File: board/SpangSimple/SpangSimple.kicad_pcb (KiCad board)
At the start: 2 copper layers, 37.5 x 43.5 mm, 3 parts

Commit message: sending off gerbers
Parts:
- removed the G*** at (182.4, 126.5) (x2)
- added BT1: Battery_Cell, SpangSimple:COINCELL_20MM_HANDSOLDER, B.Cu at (152.8, 102.2)
- added D1: LED, SpangSimple:LED_0805_HandSoldering, F.Cu at (153.9, 106.1)
- added D2: LED, SpangSimple:LED_0805_HandSoldering, F.Cu at (155.0, 107.8)
- added D3: LED, SpangSimple:LED_0805_HandSoldering, F.Cu at (156.6, 109.6)
- added D4: LED, SpangSimple:LED_0805_HandSoldering, F.Cu at (157.5, 111.3)
- added D5: LED, SpangSimple:LED_0805_HandSoldering, F.Cu at (156.4, 112.9)
- added D6: D_Schottky, Diodes_SMD:SOD-323_HandSoldering, B.Cu at (151.9, 116.9)
- added D7: LED, SpangSimple:LED_0805_HandSoldering, B.Cu at (148.1, 82.3)
- added D8: LED, SpangSimple:LED_0805_HandSoldering, B.Cu at (140.0, 91.4)
- added F1: Fuse, Fuse_Holders_and_Fuses:Fuse_SMD1206_HandSoldering, B.Cu at (145.5, 114.6)
- added G***: LOGO, LOGO, F.Cu at (182.5, 126.4)
- added G***: LOGO, LOGO, F.Cu at (182.4, 126.5)
- added R1: R, Resistors_SMD:R_0805_HandSoldering, B.Cu at (169.1, 99.8)
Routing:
- net +BATT: track 0.00 -> 80.7 mm, vias 0 -> 1
- net Net-(BT1-Pad1): track 0.00 -> 53.4 mm
- net Net-(D7-Pad1): track 0.00 -> 44.9 mm
- net GND: track 0.00 -> 29.7 mm, vias 0 -> 3
- net Net-(D6-Pad2): track 0.00 -> 4.26 mm
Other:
- net class Default: clearance 0.1 -> 0.2032
- rule trace_clearance: 0.1 -> 0.2032
- board text added: "grant"
- board text added: "jerge"
- board text added: "sincity assassin"

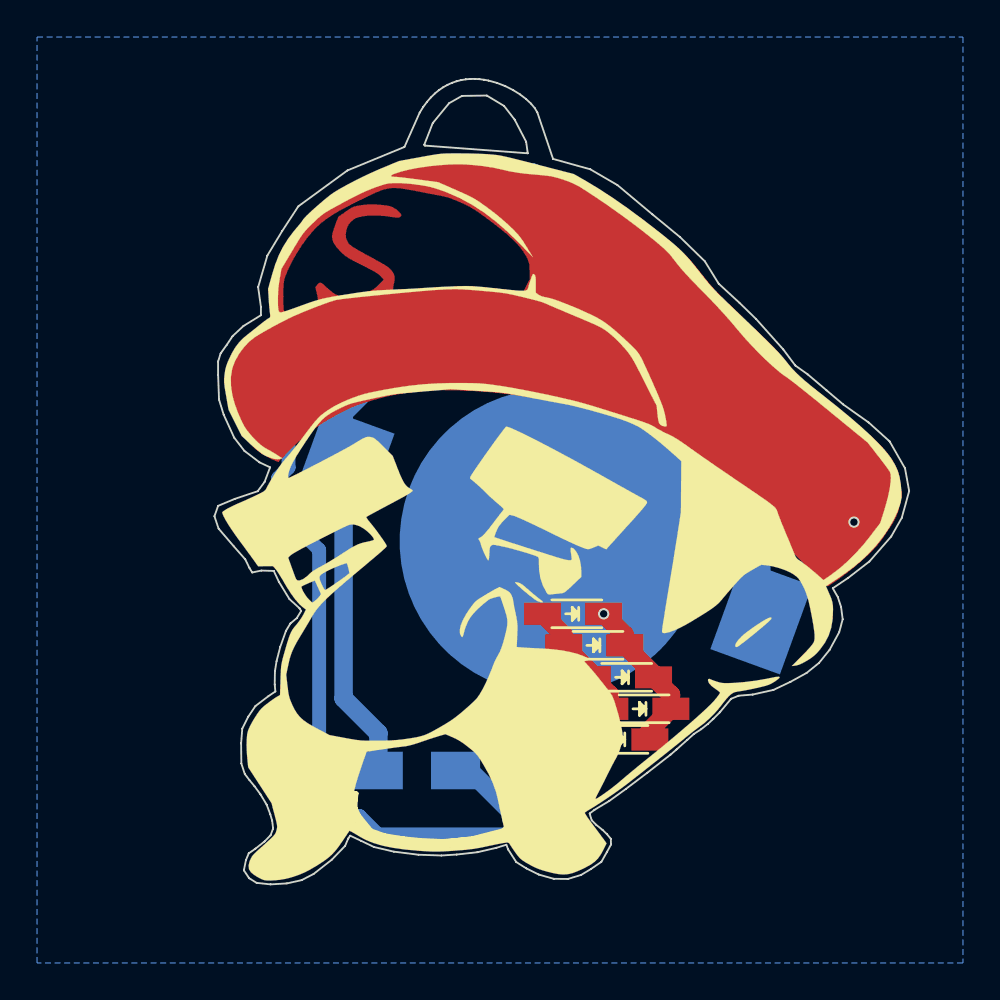
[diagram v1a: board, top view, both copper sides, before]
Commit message: removed unecessary fuse, repositioned things on board
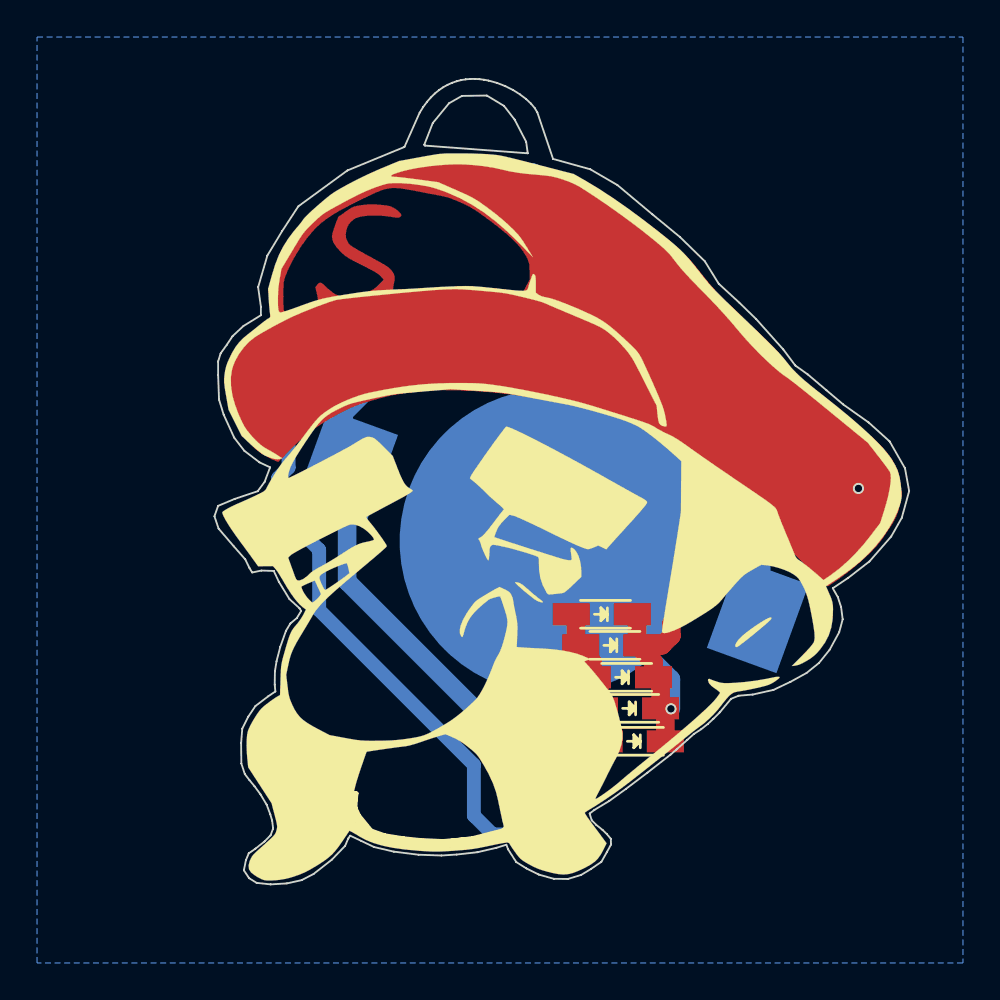
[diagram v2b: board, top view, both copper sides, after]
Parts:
- removed F1: Fuse, Fuse_Holders_and_Fuses:Fuse_SMD1206_HandSoldering
- D7, D8: footprint SpangSimple:LED_0805_HandSoldering -> SpangSimple:LED_0603_Handsoldering
- moved D1 1.55 mm to (155.4, 106.2)
- moved D2 0.91 mm to (156.0, 107.8)
- moved R1 0.90 mm to (168.4, 100.3), turned to 45 degrees
- moved D5 0.84 mm to (157.2, 113.0)
- moved D4 0.56 mm to (157.0, 111.3)
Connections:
- D6 pad 2: Net-(D6-Pad2) -> Net-(BT1-Pad1)
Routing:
- net GND: track 29.7 -> 49.6 mm, vias 3 -> 2
- net Net-(BT1-Pad1): track 53.4 -> 61.3 mm
- net +BATT: track 80.7 -> 74.7 mm
- net Net-(D6-Pad2): track 4.26 -> 0.00 mm
- net Net-(D7-Pad1): track 44.9 -> 46.4 mm
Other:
- board text added: "+"
- board text added: "-"
- board text added: "0x76696e657361756365"
- board text added: "TMG'20"
- board text removed: "JLCJLCJLCJLC"

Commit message: removed programming stuff, getting ready for final revision. Just needs last checks
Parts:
- added F1: Fuse, Resistors_SMD:R_0603_HandSoldering, B.Cu at (142.0, 115.8)
- moved R1 1.08 mm to (169.2, 101.1)
- moved D7 0.99 mm to (148.1, 83.3), turned to 160 degrees
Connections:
- BT1 pad 2: GND -> Net-(BT1-Pad2)
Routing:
- net Net-(BT1-Pad2): track 0.00 -> 18.5 mm
- net Net-(BT1-Pad1): track 61.3 -> 69.9 mm
- net Net-(D7-Pad1): track 46.4 -> 42.9 mm
- net +BATT: track 74.7 -> 72.6 mm
- net GND: track 49.6 -> 50.7 mm
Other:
- board text added: "hi chat"
- board text removed: "0x76696e657361756365"
- board text removed: "TMG'20"

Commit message: kfdjkd
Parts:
- F1: value Fuse -> Polyfuse
- moved D6 12.8 mm to (139.2, 115.1), turned to 315 degrees
- moved D8 2.87 mm to (142.5, 90.0)
- moved F1 1.76 mm to (143.4, 114.8), turned to 225 degrees
- moved D7 0.24 mm to (148.2, 83.1), turned to 340 degrees
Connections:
- F1 pad 1: Net-(BT1-Pad2) -> GND
- F1 pad 2: GND -> Net-(BT1-Pad2)
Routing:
- net Net-(BT1-Pad1): track 69.9 -> 21.3 mm
- net Net-(BT1-Pad2): track 18.5 -> 29.4 mm
- net +BATT: track 72.6 -> 75.6 mm
- net Net-(D7-Pad1): track 42.9 -> 45.7 mm
- net GND: track 50.7 -> 48.5 mm
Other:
- board text added: "CC"
- board text added: "CC Attr. ShareAlike 4.0 Int."
- board text added: "REMOVE BATTERY WHEN NOT IN USE"
